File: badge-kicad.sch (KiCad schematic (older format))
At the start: 96 parts, among them J2 JTAG, P1 TM1000, P2 CONN_02X20, P3 FTDI BACKUP, P4 Molex 105017-0001 USB B, Q1 MNBT3904, SW1 SW_PUSH, U1 WS2812B, U10 WS2812B, U11 WS2812B, U12 WS2812B, U13 MKW01Z128, U14 FT232RL SSOP, U15 TPS76333, U16 MCP73831T-2ACI/OT, U2 WS2812B, U3 WS2812B, U4 WS2812B, U5 WS2812B, U6 WS2812B, U7 WS2812B, U8 WS2812B, U9 WS2812B, Y1 AWSCR-XTAL

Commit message: replace parts with MF parts to save money, add power switch
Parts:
- removed P4: Molex 105017-0001 USB B, Connectors:USB_Micro-B, symbol USB_OTG-RESCUE-badge-kicad
- removed Q1: MNBT3904, TO_SOT_Packages_SMD:SOT-23, symbol Q_NPN_BCE
- removed R4: 120, Resistors_SMD:R_0805, symbol R
- added P4: USB_MICRO_RIGHT, MF_Connectors_MICROUSB-RIGHT, symbol USB_MICRO_RIGHT
- added Q1: NPN_BJT_SOT-23-3, MF_Discrete_Semiconductor_SOT-23-3, symbol NPN_BJT_SOT-23-3
- added SW2: SW_SPDT, symbol SW_SPDT
- D2: value BLUE SDIO -> GREEN SDIO
- U1, U10, U11, U12, U2, U3, U4, U5, U6, U7, U8, U9: footprint LEDs:LED_WS2812B-PLCC4 -> MF_LEDs_WS2812B
- U15: value TPS76333 -> MF-REG-SOT235-3.3V-300mA
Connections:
- wire segments 365 -> 381
- no-connect marks 57 -> 58
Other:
- note added: "LDO 76333 (TLV70233)\npre-programmed for 3.3V OUT, 300mA\nno FB resistors\nC13 should be X5R or X7R ceramic\n"
- note removed: "LDO 76333 is \npre-programmed for 3.3V OUT, 150mA\nno FB resistors\n"
- moved on the sheet: TP4, TP5, W4

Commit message: rebuild RF section to match KW01 dev board
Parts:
- removed C23: 6.8pF, Capacitors_SMD:C_0805_HandSoldering, symbol CP
- removed C24: 100pF, Capacitors_SMD:C_0805_HandSoldering, symbol CP
- removed C25: 7.5pF, Capacitors_SMD:C_0805_HandSoldering, symbol CP
- removed C26: 5.6pF, Capacitors_SMD:C_0805_HandSoldering, symbol CP
- removed C27, C28: 1.2pF, Capacitors_SMD:C_0805_HandSoldering, symbol CP
- removed C29: 2.0pF, Capacitors_SMD:C_0805_HandSoldering, symbol CP
- removed L1: 0.0047 uH, Inductors_NEOSID:Neosid_Inductor_SM1206, symbol INDUCTOR
- removed L4: 15 NH, Inductors_NEOSID:Neosid_Inductor_SM1206, symbol INDUCTOR
- added C16: 220pF, symbol C
- added C18: 0.1uF, symbol C
- added C19: 2pF, symbol C
- added C23: 6.8pF, symbol C
- added C24: 7.5pF, symbol C
- added C25: 5.6pF, symbol C
- added C26: 100pF, symbol C
- added C27: 1.2pF, symbol C
- added C28: 3.3pF, symbol C
- added L1: 4.7nH, symbol L
- added L2: 33nH, symbol L
- added L5: 15nH, symbol L
- renumbered L2 to L3, L3 to L4
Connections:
- net GND: now also C16.2, C18.2, C19.2, C24.2, C25.2, C27.2, C28.2
- net at U13.39 (RFIO(RF)): now also L1.1
- net VR_PA: now reaches U13.42 (VR_PA_(RF))
- net VR_PA: now also C16.1, C18.1, L2.1
- net at L3.1: now also C23.1
- net at L3.2, L4.1: now also C24.1
- net at L4.2: now also C25.1, C26.2
- net at A1.2 (FEED): now also C28.1, L5.2
- new net: C19.1, C23.2, L1.2, L2.2
- new net: C26.1, C27.1, L5.1
- no-connect marks 58 -> 57
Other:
- note added: "Exit Shield\nat this point\n"
- note added: "L5, C27, C28 as close to antenna as possible per wurth spec"
- note added: "rev1 did not connect VR_PA and it’s cap/inductor pair\n"
- note removed: "Must be \n50 Ohm Line\n"
- note removed: "RFIO_EXT"
- moved on the sheet: A1, L3, W3

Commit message: checkpoint v2 board
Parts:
- removed W4: LED_DATA_OUT, Measurement_Points:Measurement_Point_Round-TH_Small, symbol TEST_1P
- added C29: 1uF, Capacitors_SMD:C_0805_HandSoldering, symbol C
- added H1, H2, H3, H4, H5, H6: CONN_01X01, Mounting_Holes:MountingHole_3.2mm_M3_DIN965, symbol CONN_01X01
- added P5: LED OUT, Pin_Headers:Pin_Header_Straight_1x03, symbol CONN_01X03
- C1, C10, C11, C12, C2, C20, C21, C3, C4, C5, C6, C7, C8, C9: value 100nF -> 0.1uF
- C14, C15: footprint Capacitors_SMD:C_0805_HandSoldering -> Capacitors_SMD:C_1206
- C16, C19, C23, C24, C25, C26, C27, C28: footprint (none) -> Capacitors_SMD:C_0805_HandSoldering
- C18: value 0.1uF -> 0.01uF; footprint (none) -> Capacitors_SMD:C_0805_HandSoldering
- L1, L2, L5: footprint (none) -> Inductors_NEOSID:Neosid_Inductor_SM0603CG
- L3, L4: footprint Inductors_NEOSID:Neosid_Inductor_SM1206 -> Inductors_NEOSID:Neosid_Inductor_SM0603CG
- P4: footprint MF_Connectors_MICROUSB-RIGHT -> MF_Connectors:MF_Connectors-MICROUSB-RIGHT
- Q1: footprint MF_Discrete_Semiconductor_SOT-23-3 -> MF_Discrete_Semiconductor:MF_Discrete_Semiconductor-SOT-23-3
- SW1: value SW_PUSH -> RESET; footprint Buttons_Switches_SMD:SW_SPST_B3S-1000 -> MF_Switches:MF_Switches-TACT4.2MM
- SW2: footprint (none) -> Buttons_Switches_SMD:SW_SPDT_PCM12
- U1, U10, U11, U12, U2, U3, U4, U5, U6, U7, U8, U9: footprint MF_LEDs_WS2812B -> MF_LEDs:MF_LEDs-WS2812B
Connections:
- net GND: now also C29.2, H1.1 (P1), H2.1 (P1), H3.1 (P1), H4.1 (P1), H5.1 (P1), H6.1 (P1), P5.1 (P1)
- net VBAT: now also P5.3 (P3)
- net VCC: now also C29.1
- net at U12.P$2 (DOUT): now also P5.2 (P2)
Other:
- note added: "Mounting holes"

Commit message: new board shape, now with DAC, audio amp, and joypad
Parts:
- removed Q1: NPN_BJT_SOT-23-3, MF_Discrete_Semiconductor:MF_Discrete_Semiconductor-SOT-23-3, symbol NPN_BJT_SOT-23-3
- removed R1: 1K, Resistors_SMD:R_0805, symbol R
- removed R7: 100, Resistors_SMD:R_0805, symbol R
- removed SP1: TDK PS1720P02, jna-parts:TDK_PS1720PD2, symbol SPEAKER
- removed SW1: RESET, MF_Switches:MF_Switches-TACT4.2MM, symbol SW_PUSH
- removed W1: SPI_CH1_MOSI, Measurement_Points:Measurement_Point_Round-TH_Small, symbol TEST_1P
- removed W11: PTB1, Measurement_Points:Measurement_Point_Round-TH_Small, symbol TEST_1P
- removed W12: PTC1, Measurement_Points:Measurement_Point_Round-TH_Small, symbol TEST_1P
- removed W13: PTC3, Measurement_Points:Measurement_Point_Round-TH_Small, symbol TEST_1P
- removed W14: PTC4, Measurement_Points:Measurement_Point_Round-TH_Small, symbol TEST_1P
- removed W2: SPI_CH1_MISO, Measurement_Points:Measurement_Point_Round-TH_Small, symbol TEST_1P
- removed W3: SPI_CH1_SCLK, Measurement_Points:Measurement_Point_Round-TH_Small, symbol TEST_1P
- removed W8: PTD6, Measurement_Points:Measurement_Point_Round-TH_Small, symbol TEST_1P
- removed Y1: AWSCR-XTAL, Crystals:AWSCR_XTAL, symbol AWSCR-XTAL
- added C33: 11pF, Capacitors_SMD:C_0805_HandSoldering, symbol C
- added SW1: RESET, MF_Switches:MF_Switches-TACT4.2MM, symbol TACT_4.2MM
- added SW4: UP, MF_Switches:MF_Switches-TACT4.2MM, symbol TACT_4.2MM
- added SW5: DN, MF_Switches:MF_Switches-TACT4.2MM, symbol TACT_4.2MM
- added SW6: LEFT, MF_Switches:MF_Switches-TACT4.2MM, symbol TACT_4.2MM
- added SW7: RIGHT, MF_Switches:MF_Switches-TACT4.2MM, symbol TACT_4.2MM
- added SW8: ENTER, MF_Switches:MF_Switches-TACT4.2MM, symbol TACT_4.2MM
- added TP10, TP2: GND, Measurement_Points:Measurement_Point_Round-TH_Small, symbol TEST
- added TP17: SPI_CH1_SCLK, Measurement_Points:Measurement_Point_Round-TH_Small, symbol TEST
- added TP18: CLOCKOUT, Measurement_Points:Measurement_Point_Round-TH_Small, symbol TEST
- added TP19: SPI_CH1_MOSI, Measurement_Points:Measurement_Point_Round-TH_Small, symbol TEST
- added TP20: SPI_CH1_MISO, Measurement_Points:Measurement_Point_Round-TH_Small, symbol TEST
- added TP3, TP9: VCC, Measurement_Points:Measurement_Point_Round-TH_Small, symbol TEST
- added Y1: EXS00A-CS02368, jna-parts:Crystal_EXS00A-CS02368, symbol Crystal_GND24
- C17: value 100uF -> 11pF
- P5: value LED OUT -> LED OUT (DNP)
- SW2: value SW_SPDT -> POWERON
- TP1, TP4, TP5: footprint Measurement_Points:Measurement_Point_Square-TH_Small -> Measurement_Points:Measurement_Point_Round-TH_Small
- renumbered P1 to SW3
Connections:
- net CLOCKOUT: now also TP18.1
- net DISP_DC: no longer U13.16 (PTA19)
- net DISP_SCK: now also TP17.1
- net DISP_SDI(MOSI): now also TP19.1
- net DISP_SDO(MISO): now also TP20.1
- net GND: now also C33.2, SW1.P$1, SW1.P$3, SW4.P$1, SW4.P$2, SW5.P$1, SW5.P$2, SW6.P$1, SW6.P$2, SW7.P$1, SW7.P$2, SW8.P$3, SW8.P$4, TP10.1, TP2.1, Y1.2, Y1.4; no longer H1.1 (P1), H2.1 (P1), H3.1 (P1), H4.1 (P1), H5.1 (P1), H6.1 (P1)
- net LEDS_IN: no longer C17.1
- net PWM_SOUND: no longer U13.18 (PTB1), U13.25 (PTC2)
- net RESET_TGTMCU: now also SW1.P$2, SW1.P$4
- net RF_RESET: now also U13.18 (PTB1), U13.48 (RESET(RF)); no longer U13.9 (PTE30)
- net VCC: now also TP3.1, TP9.1
- net SWENTER: now reaches TP1.1, U13.12 (PTA4)
- net SWENTER: now also SW8.P$1, SW8.P$2
- net SWDN: now reaches U13.23 (PTC4)
- net SWDN: now also SW5.P$3, SW5.P$4
- net SWR: now reaches U13.24 (PTC1)
- net SWR: now also SW7.P$3, SW7.P$4
- net DIO0: now reaches U13.26 (PTC3)
- net DIO0: now also U13.49 (DIO0/PTE2/SPI1_SCK_(RF))
- net at U13.46 (XTA(RF)): now also C33.1, Y1.3
- net at U13.47 (XTB(RF)): now also C17.1, Y1.1
- new net DACOUT: U13.9 (PTE30)
- new net SWL: SW6.P$3, SW6.P$4, U13.25 (PTC2)
- new net SWUP: SW4.P$3, SW4.P$4, U13.16 (PTA19)
- no-connect marks 57 -> 62
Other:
- note added: "500mA charger"
- note added: "Extra Test Pins\n"
- note added: "REVISION 2 1/27/2017"
- note removed: "CHARGE RATE\n10k=100mA\n5.0K=200mA\n2.0K=500mA\n1.0K=1000mA"
- note removed: "these values\nnot tested\n"
- moved on the sheet: R2

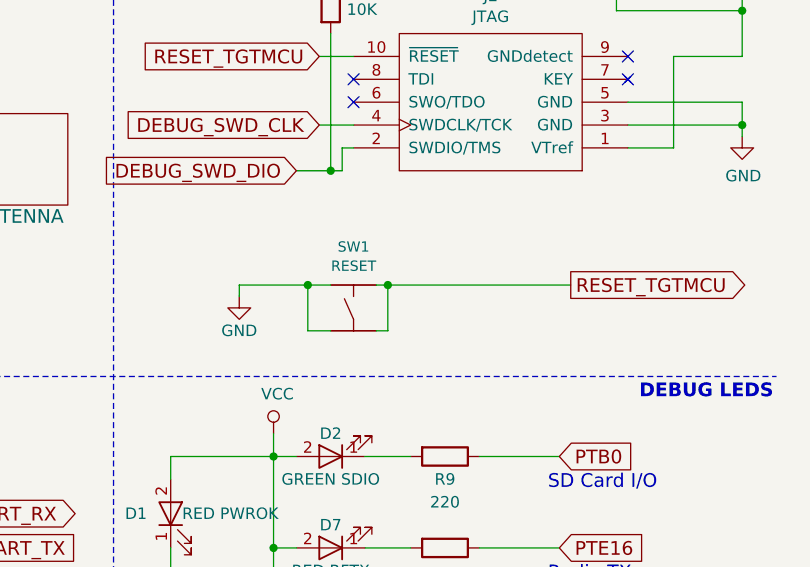
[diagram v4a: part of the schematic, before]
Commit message: Fix the reset button which was tied to ground by mistake
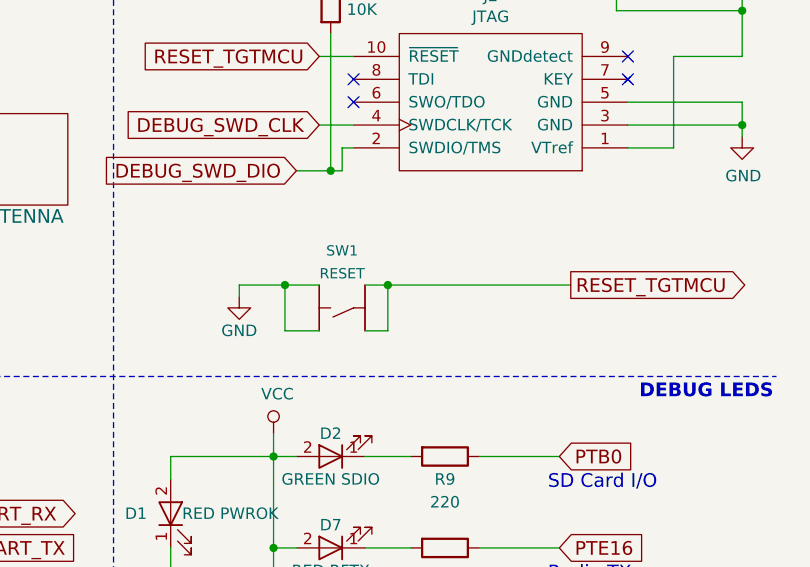
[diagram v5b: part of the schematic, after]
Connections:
- net GND: now also SW1.P$2; no longer SW1.P$3
- net RESET_TGTMCU: now also SW1.P$3; no longer SW1.P$2
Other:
- moved on the sheet: SW1
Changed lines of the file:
@@
 	6450 7700 6150 7700
 Wire Wire Line
-	14750 7300 15600 7300
-Wire Wire Line
-	14150 7300 14550 7300
+	14700 7300 15600 7300
 Wire Wire Line
 	14150 7300 14150 7350
@@
 L TACT_4.2MM SW1
 U 1 1 588F4E86
-P 14650 7400
-F 0 "SW1" H 14650 7667 45  0000 C CNN
-F 1 "RESET" H 14650 7583 45  0000 C CNN
-F 2 "MF_Switches:MF_Switches-TACT4.2MM" H 14680 7550 20  0001 C CNN
-F 3 "" H 14650 7400 60  0001 C CNN
-	1    14650 7400
-	1    0    0    -1
-$EndComp
-Wire Wire Line
-	14800 7300 14800 7500
-Wire Wire Line
-	14800 7500 14750 7500
+P 14600 7400
+F 0 "SW1" V 14850 7400 45  0000 C CNN
+F 1 "RESET" V 14750 7400 45  0000 C CNN
+F 2 "MF_Switches:MF_Switches-TACT4.2MM" H 14630 7550 20  0001 C CNN
+F 3 "" H 14600 7400 60  0001 C CNN
+	1    14600 7400
+	0    -1   -1   0
+$EndComp
+Wire Wire Line
+	14800 7500 14800 7300
+Wire Wire Line
+	14700 7500 14800 7500
 Connection ~ 14800 7300
-Wire Wire Line
-	14550 7500 14450 7500
-Wire Wire Line
-	14450 7500 14450 7300
-Connection ~ 14450 7300
 Text GLabel 3650 10200 3    60   Output ~ 0
 DIO0
@@
 NoConn ~ 14750 3750
 NoConn ~ 15700 3750
+Wire Wire Line
+	14150 7300 14500 7300
+Wire Wire Line
+	14350 7300 14350 7500
+Wire Wire Line
+	14350 7500 14500 7500
+Connection ~ 14350 7300
 $EndSCHEMATC

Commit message: swap PTD7 and PTB1
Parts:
- added H7: CONN_01X01, Mounting_Holes:MountingHole_3.2mm_M3_DIN965, symbol CONN_01X01
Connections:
- net RF_RESET: now also U13.31 (PTD7/SPI0_MISO); no longer U13.18 (PTB1)
- net PTD7 renamed PTB1
- net PTB1: now also U13.18 (PTB1); no longer U13.31 (PTD7/SPI0_MISO)
- no-connect marks 62 -> 63
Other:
- moved on the sheet: H3, H4, H5, H6
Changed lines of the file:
@@
 DEBUG LEDS\n\n
 Text GLabel 2100 9300 0    60   Output ~ 0
-RF_RESET
+PTB1
 Text GLabel 2100 9450 0    60   Output ~ 0
 PTB0
@@
 $EndComp
 Text GLabel 6450 8150 2    60   Output ~ 0
-PTD7
+RF_RESET
 Text Notes 15500 8950 0    60   ~ 0
 Radio RX
@@
 $EndComp
 Text GLabel 15550 8800 2    60   Input ~ 0
-PTD7
+PTB1
 Text GLabel 11650 600  0    60   Input ~ 0
 VBAT
@@
 L CONN_01X01 H5
 U 1 1 5866FEEA
-P 14750 5100
-F 0 "H5" V 14715 5012 50  0000 R CNN
-F 1 "CONN_01X01" V 14624 5012 50  0000 R CNN
-F 2 "Mounting_Holes:MountingHole_3.2mm_M3_DIN965" H 14750 5100 50  0001 C CNN
-F 3 "" H 14750 5100 50  0000 C CNN
-	1    14750 5100
+P 14750 4750
+F 0 "H5" V 14715 4662 50  0000 R CNN
+F 1 "CONN_01X01" V 14624 4662 50  0000 R CNN
+F 2 "Mounting_Holes:MountingHole_3.2mm_M3_DIN965" H 14750 4750 50  0001 C CNN
+F 3 "" H 14750 4750 50  0000 C CNN
+	1    14750 4750
 	0    -1   -1   0
 $EndComp
@@
 L CONN_01X01 H3
 U 1 1 586701C1
-P 14750 4350
-F 0 "H3" V 14715 4262 50  0000 R CNN
-F 1 "CONN_01X01" V 14624 4262 50  0000 R CNN
-F 2 "Mounting_Holes:MountingHole_3.2mm_M3_DIN965" H 14750 4350 50  0001 C CNN
-F 3 "" H 14750 4350 50  0000 C CNN
-	1    14750 4350
+P 14750 4150
+F 0 "H3" V 14715 4062 50  0000 R CNN
+F 1 "CONN_01X01" V 14624 4062 50  0000 R CNN
+F 2 "Mounting_Holes:MountingHole_3.2mm_M3_DIN965" H 14750 4150 50  0001 C CNN
+F 3 "" H 14750 4150 50  0000 C CNN
+	1    14750 4150
 	0    -1   -1   0
 $EndComp
@@
 L CONN_01X01 H4
 U 1 1 586705B8
-P 15700 4350
-F 0 "H4" V 15665 4262 50  0000 R CNN
-F 1 "CONN_01X01" V 15574 4262 50  0000 R CNN
-F 2 "Mounting_Holes:MountingHole_3.2mm_M3_DIN965" H 15700 4350 50  0001 C CNN
-F 3 "" H 15700 4350 50  0000 C CNN
-	1    15700 4350
+P 15700 4150
+F 0 "H4" V 15665 4062 50  0000 R CNN
+F 1 "CONN_01X01" V 15574 4062 50  0000 R CNN
+F 2 "Mounting_Holes:MountingHole_3.2mm_M3_DIN965" H 15700 4150 50  0001 C CNN
+F 3 "" H 15700 4150 50  0000 C CNN
+	1    15700 4150
 	0    -1   -1   0
 $EndComp
@@
 L CONN_01X01 H6
 U 1 1 5867070A
-P 15700 5100
-F 0 "H6" V 15665 5012 50  0000 R CNN
-F 1 "CONN_01X01" V 15574 5012 50  0000 R CNN
-F 2 "Mounting_Holes:MountingHole_3.2mm_M3_DIN965" H 15700 5100 50  0001 C CNN
-F 3 "" H 15700 5100 50  0000 C CNN
-	1    15700 5100
+P 15700 4750
+F 0 "H6" V 15665 4662 50  0000 R CNN
+F 1 "CONN_01X01" V 15574 4662 50  0000 R CNN
+F 2 "Mounting_Holes:MountingHole_3.2mm_M3_DIN965" H 15700 4750 50  0001 C CNN
+F 3 "" H 15700 4750 50  0000 C CNN
+	1    15700 4750
 	0    -1   -1   0
 $EndComp
-NoConn ~ 15700 4550
-NoConn ~ 15700 5300
-NoConn ~ 14750 5300
-NoConn ~ 14750 4550
+NoConn ~ 15700 4350
+NoConn ~ 15700 4950
+NoConn ~ 14750 4950
+NoConn ~ 14750 4350
 NoConn ~ 14750 3750
 NoConn ~ 15700 3750
@@
 	14350 7500 14500 7500
 Connection ~ 14350 7300
+$Comp
+L CONN_01X01 H7
+U 1 1 58997660
+P 14750 5250
+F 0 "H7" V 14715 5162 50  0000 R CNN
+F 1 "CONN_01X01" V 14624 5162 50  0000 R CNN
+F 2 "Mounting_Holes:MountingHole_3.2mm_M3_DIN965" H 14750 5250 50  0001 C CNN
+F 3 "" H 14750 5250 50  0000 C CNN
+	1    14750 5250
+	0    -1   -1   0
+$EndComp
+NoConn ~ 14750 5450
 $EndSCHEMATC

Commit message: Final rev2, clean up rev1
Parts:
- C18, C19, C23, C24: footprint Capacitors_SMD:C_0805_HandSoldering -> Capacitors_SMD:C_0603_HandSoldering
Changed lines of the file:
@@
 F 0 "C19" H 7915 7096 50  0000 L CNN
 F 1 "2pF" H 7915 7005 50  0000 L CNN
-F 2 "Capacitors_SMD:C_0805_HandSoldering" H 7838 6900 50  0001 C CNN
+F 2 "Capacitors_SMD:C_0603_HandSoldering" H 7838 6900 50  0001 C CNN
 F 3 "" H 7800 7050 50  0000 C CNN
 	1    7800 7050
@@
 F 0 "C24" H 9915 7096 50  0000 L CNN
 F 1 "7.5pF" H 9915 7005 50  0000 L CNN
-F 2 "Capacitors_SMD:C_0805_HandSoldering" H 9838 6900 50  0001 C CNN
+F 2 "Capacitors_SMD:C_0603_HandSoldering" H 9838 6900 50  0001 C CNN
 F 3 "" H 9800 7050 50  0000 C CNN
 	1    9800 7050
@@
 F 0 "C23" V 8148 6750 50  0000 C CNN
 F 1 "6.8pF" V 8239 6750 50  0000 C CNN
-F 2 "Capacitors_SMD:C_0805_HandSoldering" H 8438 6600 50  0001 C CNN
+F 2 "Capacitors_SMD:C_0603_HandSoldering" H 8438 6600 50  0001 C CNN
 F 3 "" H 8400 6750 50  0000 C CNN
 	1    8400 6750
@@
 F 0 "C18" H 7600 5750 50  0000 L CNN
 F 1 "0.01uF" H 7500 5650 50  0000 L CNN
-F 2 "Capacitors_SMD:C_0805_HandSoldering" H 7488 5650 50  0001 C CNN
+F 2 "Capacitors_SMD:C_0603_HandSoldering" H 7488 5650 50  0001 C CNN
 F 3 "" H 7450 5800 50  0000 C CNN
 	1    7450 5800
@@
 $EndComp
 $Comp
-L GND #PWR046
+L GND #PWR040
 U 1 1 588B02C8
 P 16400 2950
-F 0 "#PWR046" H 16400 2700 50  0001 C CNN
+F 0 "#PWR040" H 16400 2700 50  0001 C CNN
 F 1 "GND" H 16405 2777 50  0000 C CNN
 F 2 "" H 16400 2950 50  0000 C CNN
@@
 $EndComp
 $Comp
-L VCC #PWR047
+L VCC #PWR041
 U 1 1 588B394B
 P 16300 1900
-F 0 "#PWR047" H 16300 1750 50  0001 C CNN
+F 0 "#PWR041" H 16300 1750 50  0001 C CNN
 F 1 "VCC" H 16317 2073 50  0000 C CNN
 F 2 "" H 16300 1900 50  0000 C CNN
@@
 	3650 3700 3650 4150
 $Comp
-L GND #PWR048
+L GND #PWR042
 U 1 1 588DEEDE
 P 3450 4000
-F 0 "#PWR048" H 3450 3750 50  0001 C CNN
+F 0 "#PWR042" H 3450 3750 50  0001 C CNN
 F 1 "GND" H 3350 4000 50  0000 C CNN
 F 2 "" H 3450 4000 50  0000 C CNN
@@
 	3450 3900 3450 4000
 $Comp
-L GND #PWR049
+L GND #PWR043
 U 1 1 588DF442
 P 3700 3500
-F 0 "#PWR049" H 3700 3250 50  0001 C CNN
+F 0 "#PWR043" H 3700 3250 50  0001 C CNN
 F 1 "GND" H 3600 3500 50  0000 C CNN
 F 2 "" H 3700 3500 50  0000 C CNN
@@
 $EndComp
 $Comp
-L GND #PWR050
+L GND #PWR044
 U 1 1 588E38CC
 P 2200 4100
-F 0 "#PWR050" H 2200 3850 50  0001 C CNN
+F 0 "#PWR044" H 2200 3850 50  0001 C CNN
 F 1 "GND" H 2205 3927 50  0000 C CNN
 F 2 "" H 2200 4100 50  0000 C CNN
@@
 Connection ~ 3200 3700
 $Comp
-L GND #PWR051
+L GND #PWR045
 U 1 1 588E4DB4
 P 4600 4050
-F 0 "#PWR051" H 4600 3800 50  0001 C CNN
+F 0 "#PWR045" H 4600 3800 50  0001 C CNN
 F 1 "GND" H 4605 3877 50  0000 C CNN
 F 2 "" H 4600 4050 50  0000 C CNN
@@
 	2200 3950 2200 4100
 $Comp
-L GND #PWR052
+L GND #PWR046
 U 1 1 588EB7C8
 P 7100 10300
-F 0 "#PWR052" H 7100 10050 50  0001 C CNN
+F 0 "#PWR046" H 7100 10050 50  0001 C CNN
 F 1 "GND" H 7105 10127 50  0000 C CNN
 F 2 "" H 7100 10300 50  0000 C CNN
